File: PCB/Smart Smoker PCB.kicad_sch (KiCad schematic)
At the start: 78 parts, among them J1 105017-0001, J2 393570002, J3 393570002, J4 393570002, J5 393570002, J6 393570002, J7 393570002, J8 Hopper, J9 Lid, Q1 Q_PMOS_GSD, Q2 25V 1.5A Trans, Q3 25V 1.5A Trans, Q4 Q_PMOS_GSD, Q5 2N7002T-7-F, Q6 2N7002T-7-F, U1 ESP32-WROOM-32UE_16MB, U2 DG409LEDY-T1-GE3, U3 MAX31855KASA, U4 AMS1117-3.3, U5 CP2102N-Axx-xQFN28, U6 LTC4412xS6

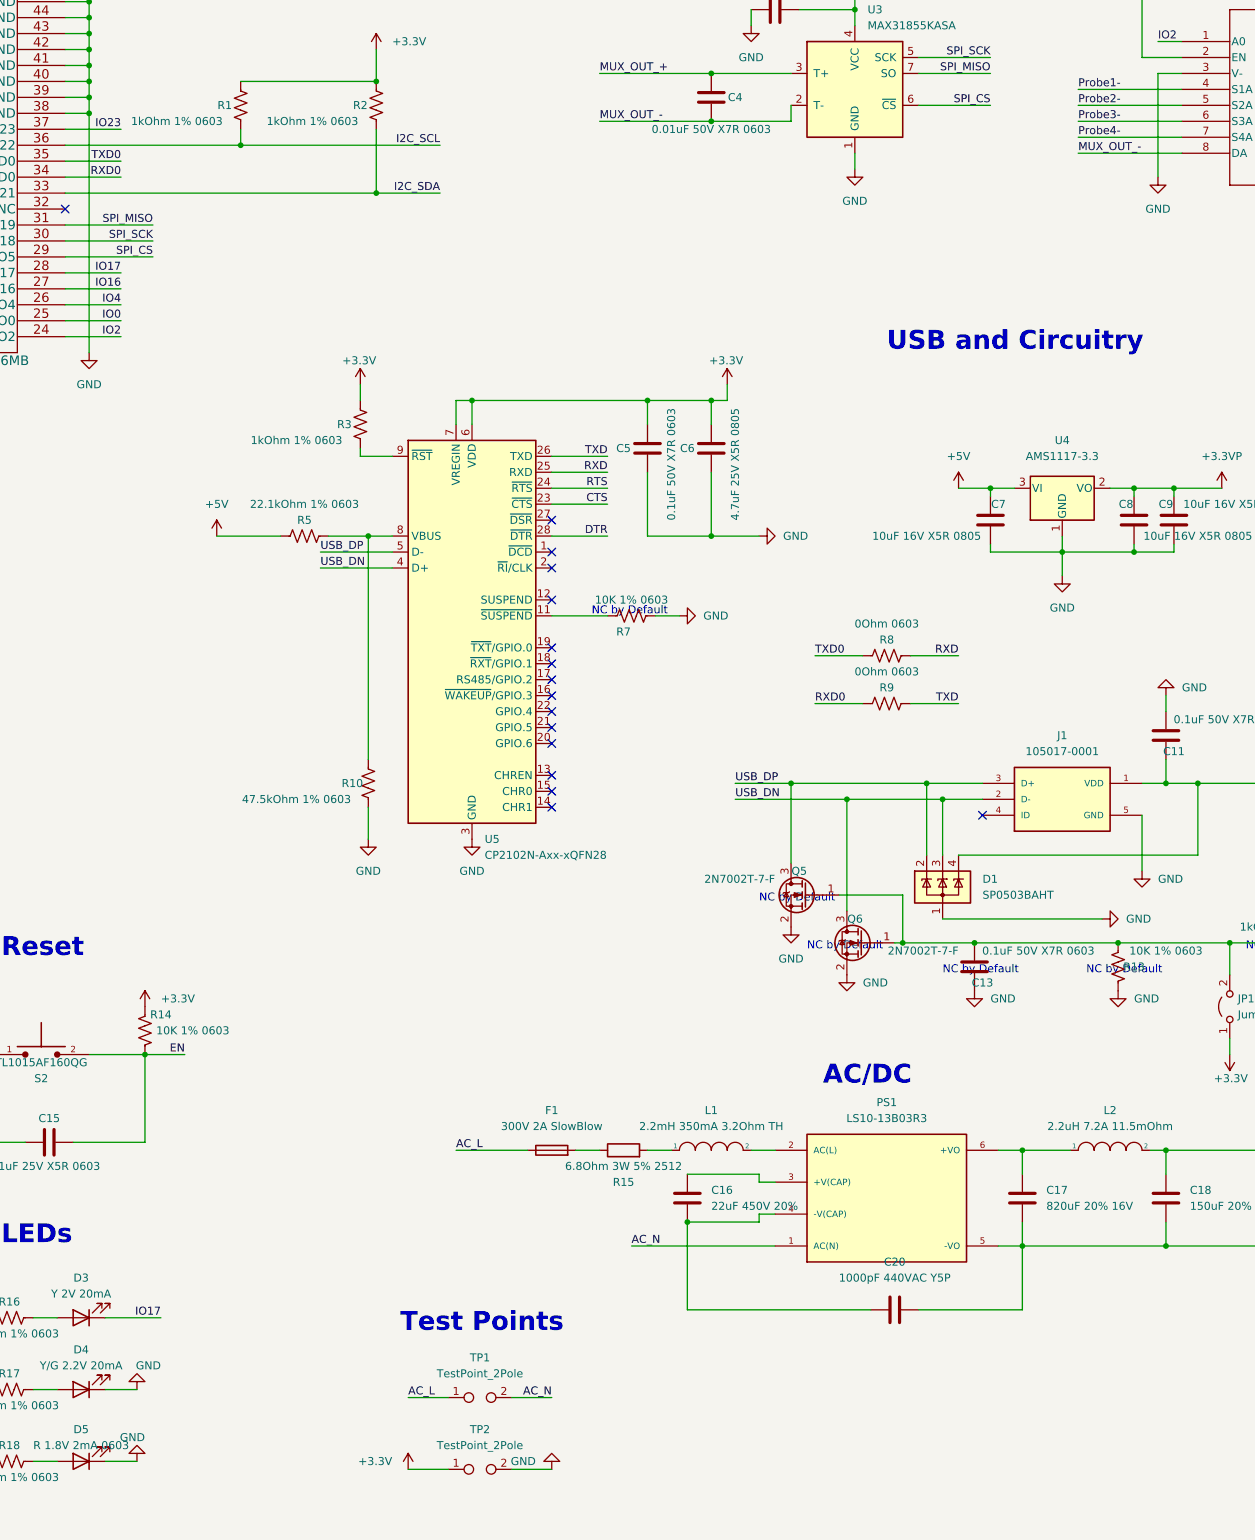
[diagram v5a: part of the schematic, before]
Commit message: 3x PCB ready for gerberization
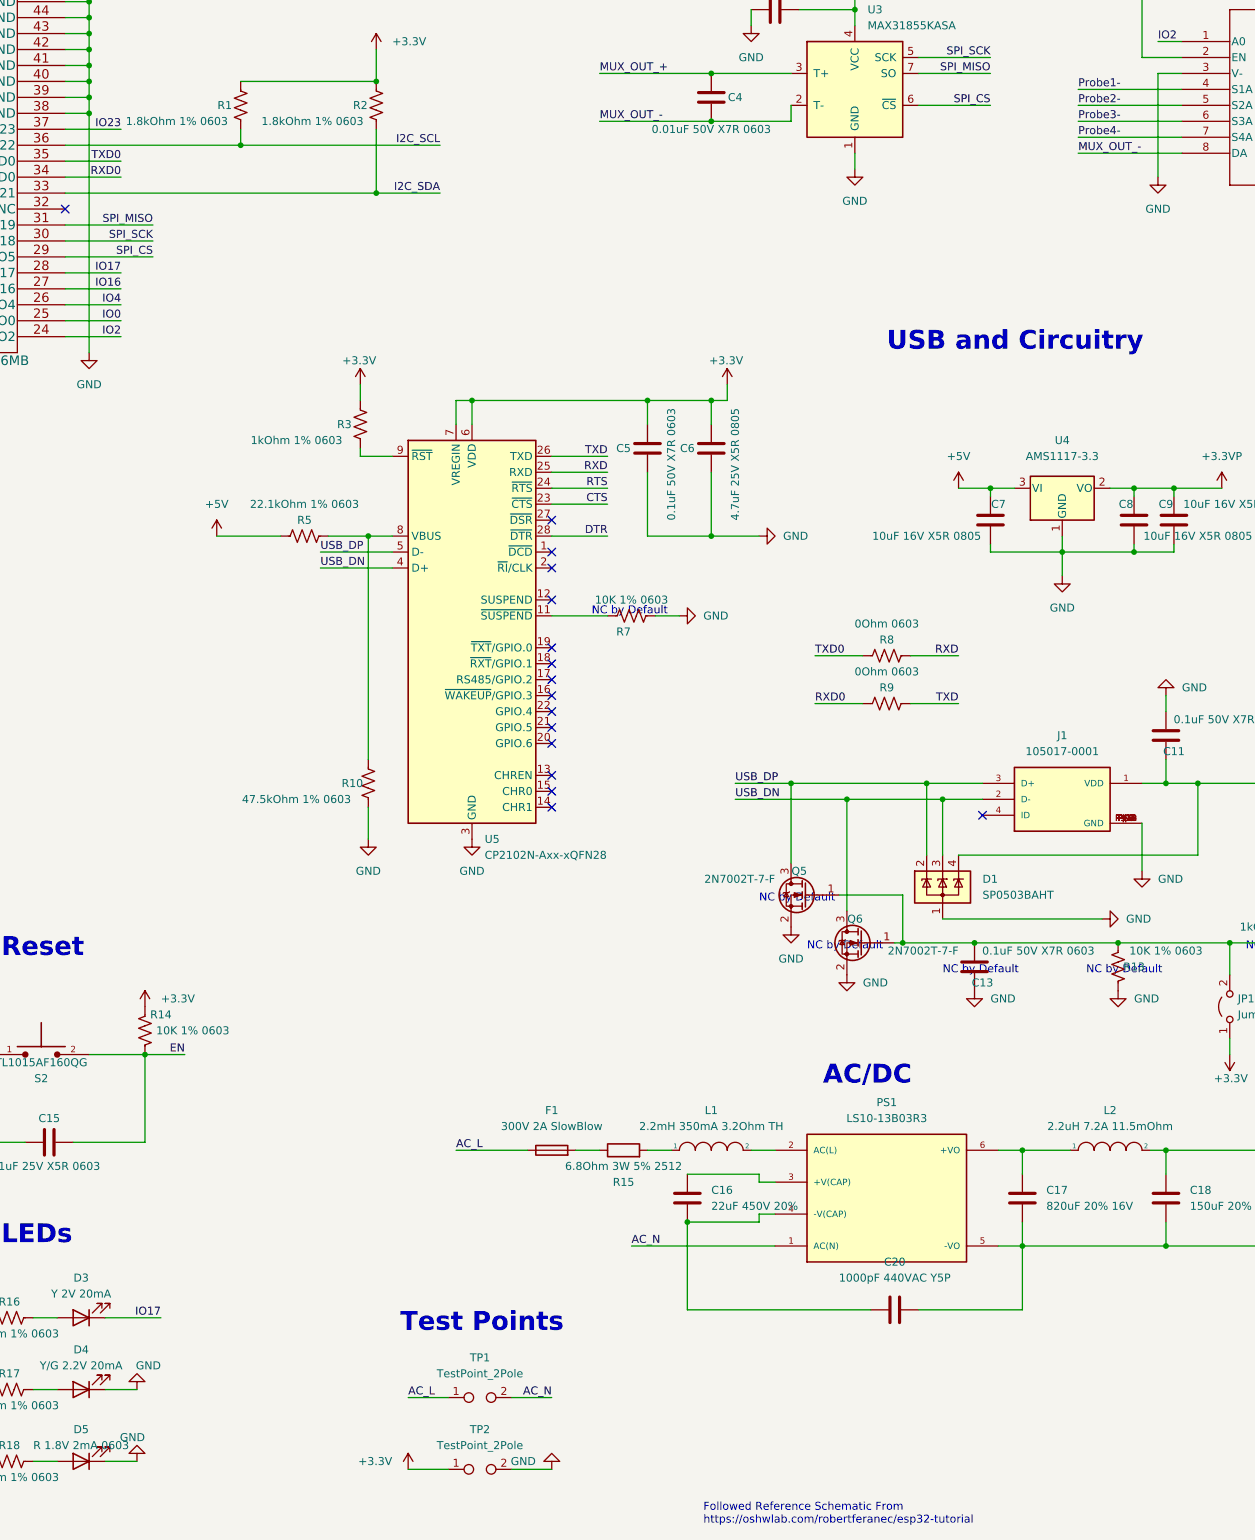
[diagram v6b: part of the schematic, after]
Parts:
- R1, R2: value 1kOhm 1% 0603 -> 1.8kOhm 1% 0603; Manufacturer Stackpole Electronics Inc -> TE Connectivity Passive Product; Manufacturer Part Number RNCP0603FTD1K00 -> CRGCQ0603F1K8; Vendor Part Number RNCP0603FTD1K00CT-ND -> A129691CT-ND
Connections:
- net GND: now also J1.P$1 (GND), J1.P$10 (GND), J1.P$11 (GND), J1.P$12 (GND), J1.P$13 (GND), J1.P$2 (GND), J1.P$8 (GND), J1.P$9 (GND)
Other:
- note added: "Followed Reference Schematic From https://oshwlab.com/robertferanec/esp32-tutorial"
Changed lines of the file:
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@@
     (stroke (width 0) (type default) (color 0 0 0 0))
   )
+  (wire (pts (xy 318.77 171.45) (xy 318.77 179.07))
+    (stroke (width 0) (type default) (color 0 0 0 0))
+  )
   (wire (pts (xy 266.7 152.4) (xy 274.32 152.4))
     (stroke (width 0) (type default) (color 0 0 0 0))
@@
     (stroke (width 0) (type default) (color 0 0 0 0))
   )
-  (wire (pts (xy 318.77 170.18) (xy 318.77 179.07))
-    (stroke (width 0) (type default) (color 0 0 0 0))
-  )
   (wire (pts (xy 252.73 101.6) (xy 252.73 104.14))
     (stroke (width 0) (type default) (color 0 0 0 0))
@@
     (effects (font (size 1.27 1.27)) (justify left bottom))
   )
+  (text "Followed Reference Schematic From\nhttps://oshwlab.com/robertferanec/esp32-tutorial"
+    (at 248.92 283.21 0)
+    (effects (font (size 1.27 1.27)) (justify left bottom))
+  )
   (text "NC by Default" (at 309.88 195.58 0)
     (effects (font (size 1.27 1.27)) (justify left bottom))
@@
     (property "Reference" "J1" (id 0) (at 306.07 157.48 0))
     (property "Value" "105017-0001" (id 1) (at 306.07 160.02 0))
-    (property "Footprint" "MOLEX_105017-0001" (id 2) (at 306.07 167.64 0)
+    (property "Footprint" "MOLEX_105017-0001" (id 2) (at 303.53 162.56 0)
       (effects (font (size 1.27 1.27)) (justify bottom) hide)
     )
@@
       (effects (font (size 1.27 1.27)) hide)
     )
-    (property "Manufacturer" "Molex" (id 4) (at 306.07 167.64 0)
+    (property "Manufacturer" "Molex" (id 4) (at 306.07 162.56 0)
       (effects (font (size 1.27 1.27)) hide)
     )
-    (property "Manufacturer Part Number" "1050170001" (id 5) (at 306.07 167.64 0)
+    (property "Manufacturer Part Number" "1050170001" (id 5) (at 307.34 162.56 0)
       (effects (font (size 1.27 1.27)) hide)
     )
-    (property "Vendor" "Digikey" (id 6) (at 306.07 167.64 0)
+    (property "Vendor" "Digikey" (id 6) (at 306.07 162.56 0)
       (effects (font (size 1.27 1.27)) hide)
     )
-    (property "Vendor Part Number" "WM1399CT-ND" (id 7) (at 306.07 167.64 0)
+    (property "Vendor Part Number" "WM1399CT-ND" (id 7) (at 306.07 162.56 0)
       (effects (font (size 1.27 1.27)) hide)
     )
@@
     (pin "4")
     (pin "5")
+    (pin "P$1")
+    (pin "P$10")
+    (pin "P$11")
+    (pin "P$12")
+    (pin "P$13")
+    (pin "P$2")
+    (pin "P$8")
+    (pin "P$9")
   )
   (symbol (lib_id "power:+3.3V") (at 252.73 101.6 0) (unit 1)
@@
     (in_bom yes) (on_board yes)
     (property "Reference" "R2" (id 0) (at 194.31 57.15 0))
-    (property "Value" "1kOhm 1% 0603" (id 1) (at 186.69 59.69 0))
+    (property "Value" "1.8kOhm 1% 0603" (id 1) (at 186.69 59.69 0))
     (property "Footprint" "Resistor_SMD:R_0603_1608Metric" (id 2) (at 195.834 56.896 90)
       (effects (font (size 1.27 1.27)) hide)
@@
       (effects (font (size 1.27 1.27)) hide)
     )
-    (property "Manufacturer" "Stackpole Electronics Inc" (id 4) (at 196.85 57.15 0)
+    (property "Manufacturer" "TE Connectivity Passive Product" (id 4) (at 196.85 57.15 0)
       (effects (font (size 1.27 1.27)) hide)
     )
-    (property "Manufacturer Part Number" "RNCP0603FTD1K00" (id 5) (at 196.85 57.15 0)
+    (property "Manufacturer Part Number" "CRGCQ0603F1K8" (id 5) (at 196.85 57.15 0)
       (effects (font (size 1.27 1.27)) hide)
     )
@@
       (effects (font (size 1.27 1.27)) hide)
     )
-    (property "Vendor Part Number" "RNCP0603FTD1K00CT-ND" (id 7) (at 196.85 57.15 0)
+    (property "Vendor Part Number" "A129691CT-ND" (id 7) (at 196.85 57.15 0)
       (effects (font (size 1.27 1.27)) hide)
     )
@@
     (in_bom yes) (on_board yes)
     (property "Reference" "R1" (id 0) (at 172.72 57.15 0))
-    (property "Value" "1kOhm 1% 0603" (id 1) (at 165.1 59.69 0))
+    (property "Value" "1.8kOhm 1% 0603" (id 1) (at 165.1 59.69 0))
     (property "Footprint" "Resistor_SMD:R_0603_1608Metric" (id 2) (at 174.244 56.896 90)
       (effects (font (size 1.27 1.27)) hide)
@@
       (effects (font (size 1.27 1.27)) hide)
     )
-    (property "Manufacturer" "Stackpole Electronics Inc" (id 4) (at 175.26 57.15 0)
+    (property "Manufacturer" "TE Connectivity Passive Product" (id 4) (at 175.26 57.15 0)
       (effects (font (size 1.27 1.27)) hide)
     )
-    (property "Manufacturer Part Number" "RNCP0603FTD1K00" (id 5) (at 175.26 57.15 0)
+    (property "Manufacturer Part Number" "CRGCQ0603F1K8" (id 5) (at 175.26 57.15 0)
       (effects (font (size 1.27 1.27)) hide)
     )
@@
       (effects (font (size 1.27 1.27)) hide)
     )
-    (property "Vendor Part Number" "RNCP0603FTD1K00CT-ND" (id 7) (at 175.26 57.15 0)
+    (property "Vendor Part Number" "A129691CT-ND" (id 7) (at 175.26 57.15 0)
       (effects (font (size 1.27 1.27)) hide)
     )
@@
     )
     (path "/e4ecb6d7-1182-4686-9857-dfce373566a8"
-      (reference "R1") (unit 1) (value "1kOhm 1% 0603") (footprint "Resistor_SMD:R_0603_1608Metric")
+      (reference "R1") (unit 1) (value "1.8kOhm 1% 0603") (footprint "Resistor_SMD:R_0603_1608Metric")
     )
     (path "/81b70cdc-fabf-4c53-a6c8-e0a49716e914"
-      (reference "R2") (unit 1) (value "1kOhm 1% 0603") (footprint "Resistor_SMD:R_0603_1608Metric")
+      (reference "R2") (unit 1) (value "1.8kOhm 1% 0603") (footprint "Resistor_SMD:R_0603_1608Metric")
     )
     (path "/46bf0c80-63a4-44ba-ada9-dbdcdbc6fa27"

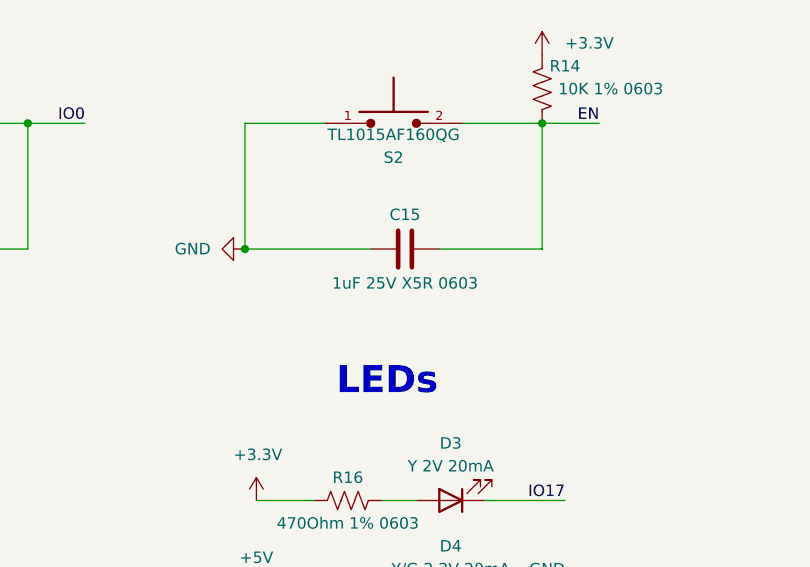
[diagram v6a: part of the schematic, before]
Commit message: MOV added to PCB1
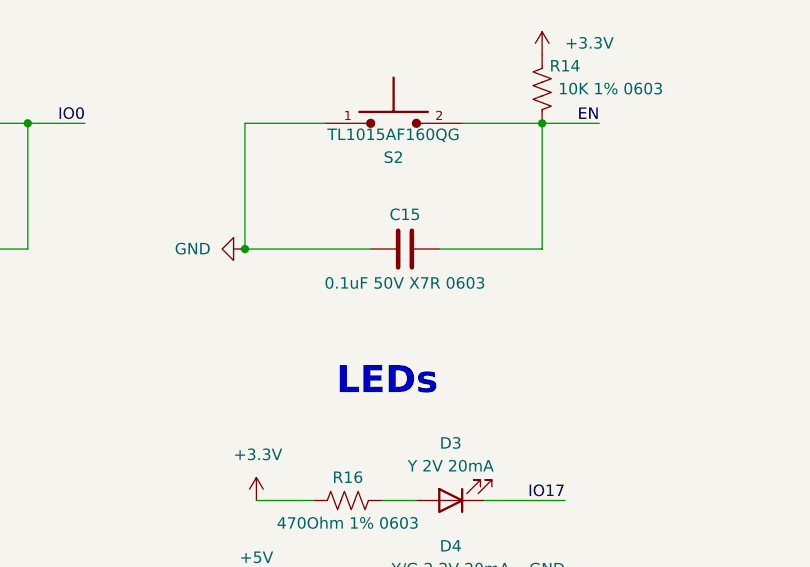
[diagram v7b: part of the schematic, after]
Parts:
- C15: value 1uF 25V X5R 0603 -> 0.1uF 50V X7R 0603; Manufacturer Part Number CL10A105KA8NNNC -> CL10B104KB8NNWC; Vendor Part Number 1276-1102-1-ND -> 1276-1935-1-ND
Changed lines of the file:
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@@
     (in_bom yes) (on_board yes)
     (property "Reference" "C15" (id 0) (at 144.78 218.44 90))
-    (property "Value" "1uF 25V X5R 0603" (id 1) (at 144.78 226.06 90))
+    (property "Value" "0.1uF 50V X7R 0603" (id 1) (at 144.78 226.06 90))
     (property "Footprint" "Capacitor_SMD:C_0603_1608Metric" (id 2) (at 140.97 223.2152 0)
       (effects (font (size 1.27 1.27)) hide)
@@
       (effects (font (size 1.27 1.27)) hide)
     )
-    (property "Manufacturer Part Number" "CL10A105KA8NNNC" (id 5) (at 144.78 222.25 0)
+    (property "Manufacturer Part Number" "CL10B104KB8NNWC" (id 5) (at 144.78 222.25 0)
       (effects (font (size 1.27 1.27)) hide)
     )
@@
       (effects (font (size 1.27 1.27)) hide)
     )
-    (property "Vendor Part Number" "1276-1102-1-ND" (id 7) (at 144.78 222.25 0)
+    (property "Vendor Part Number" "1276-1935-1-ND" (id 7) (at 144.78 222.25 0)
       (effects (font (size 1.27 1.27)) hide)
     )
@@
     )
     (path "/4c42aa9b-1713-42cd-93fa-004f6e87dbba"
-      (reference "C15") (unit 1) (value "1uF 25V X5R 0603") (footprint "Capacitor_SMD:C_0603_1608Metric")
+      (reference "C15") (unit 1) (value "0.1uF 50V X7R 0603") (footprint "Capacitor_SMD:C_0603_1608Metric")
     )
     (path "/bc2bab20-efe8-4ddb-b8ea-6e709a83fa75"

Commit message: 3x PCB ordered
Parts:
- added AE1: Antenna, Symbol:KiCad-Logo2_5mm_SilkScreen, symbol Device:Antenna
- added R16: B72214S0351K101, VARS_B72214S_15P5X5P6-7P5-2P2_TDK, symbol B72214S0351K101:B72214S0351K101
- L1: value 2.2mH 350mA 3.2Ohm TH -> 2.2mH 500mA 2.5Ohm TH; footprint Inductor_THT:L_Radial_D12.0mm_P5.00mm_Fastron_11P -> Inductor_THT:L_Radial_D10.5mm_P5.00mm_Abacron_AISR-01; Manufacturer Bourns Inc. -> Würth Elektronik; Manufacturer Part Number RLB1112V4-222J -> 7687480222; Vendor Part Number 118-RLB1112V4-222JCT-ND -> 732-7687480222-ND
- R15: footprint Resistor_SMD:R_2512_6332Metric -> Resistor_THT:R_Box_L8.4mm_W2.5mm_P5.08mm; Manufacturer TE Connectivity Passive Product -> Vishay Beyschlag/Draloric/BC Components; Manufacturer Part Number 35226R8JT -> AC03000006808JAC00; Vendor Part Number A121299CT-ND -> 749-AC03000006808JAC00CT-ND
- renumbered R16 to R17, R17 to R18, R18 to R19
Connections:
- net AC_N: now also R16.2
- net USB_DN: now also U5.5 (D-); no longer U5.4 (D+)
- net USB_DP: now also U5.4 (D+); no longer U5.5 (D-)
- net at F1.2, R15.1: now also R16.1
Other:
- note added: "ANTENNA"
